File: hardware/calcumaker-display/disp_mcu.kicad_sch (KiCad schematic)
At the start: 8 parts, among them J3 SWD TC2030-NL, U4 STM32G031K8U6

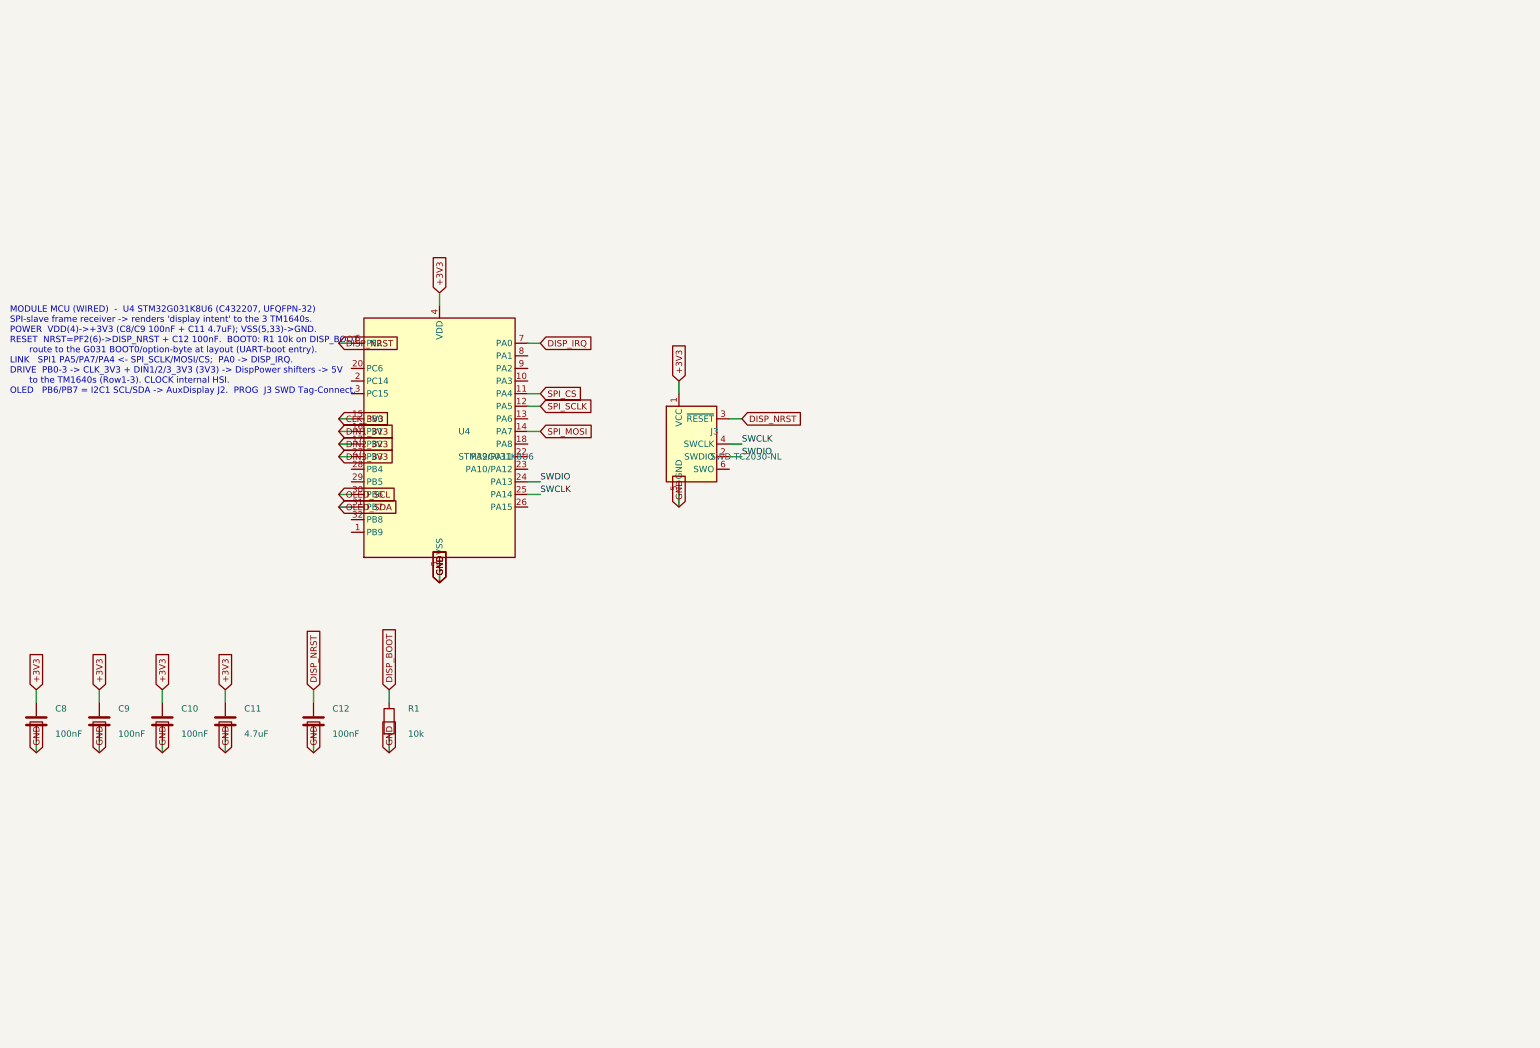
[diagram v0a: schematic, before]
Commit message: Floorplan both display PCBs and verify their schematic nets
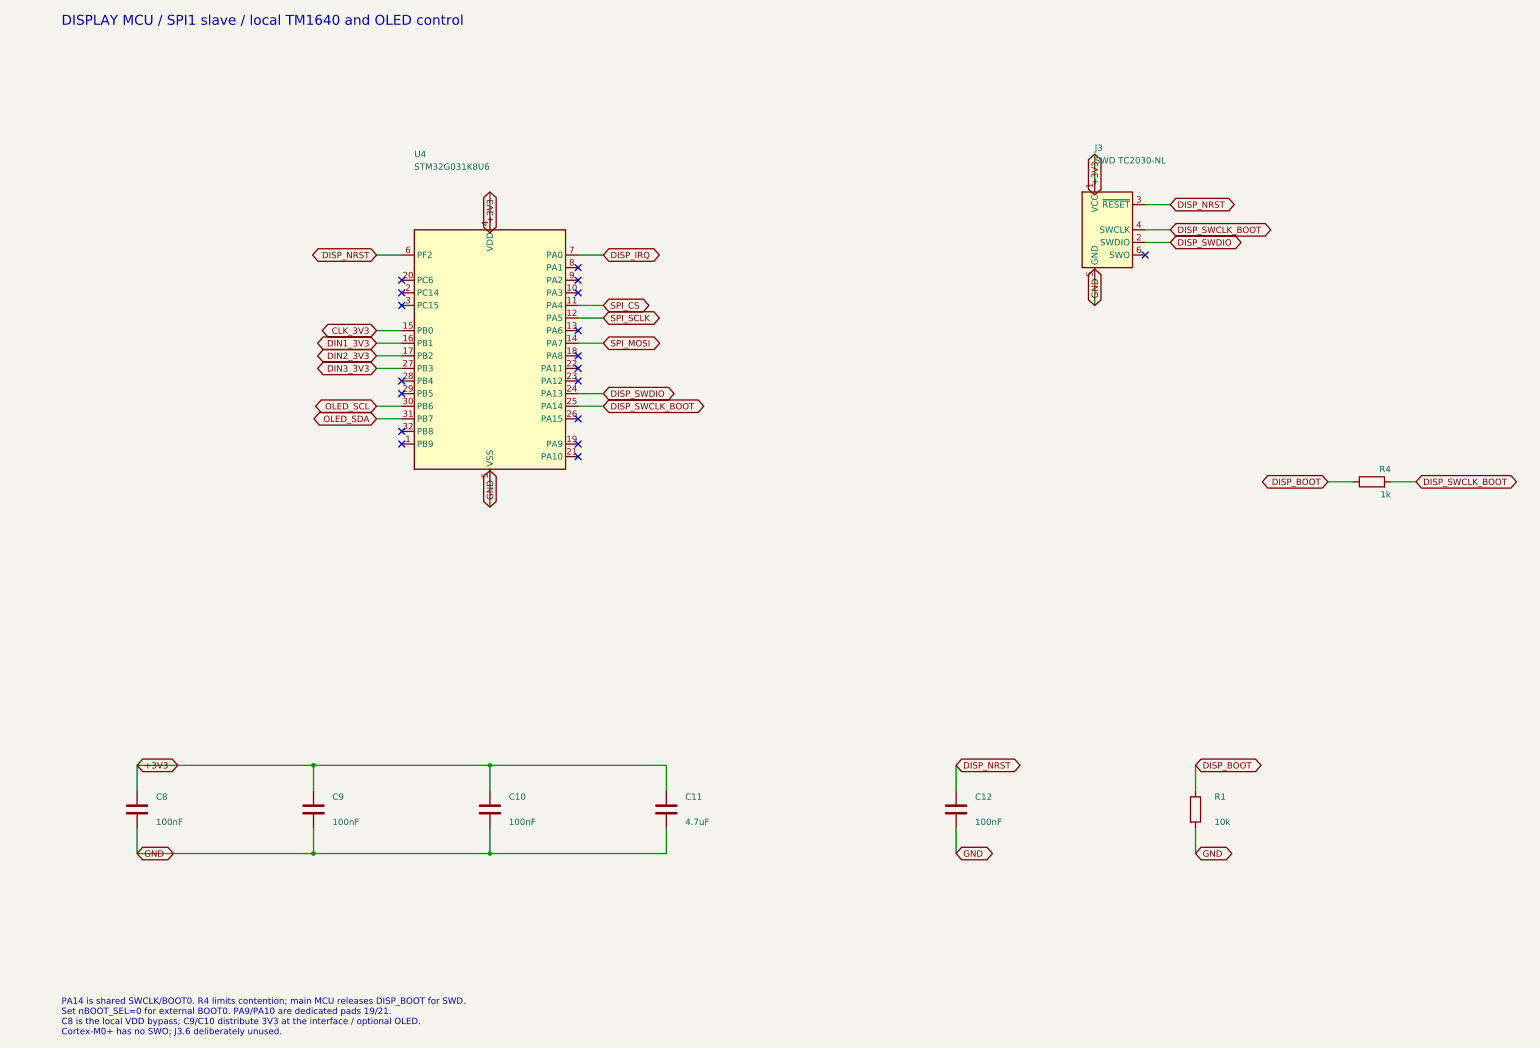
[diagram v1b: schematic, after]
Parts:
- added R4: 1k, Resistor_SMD:R_0402_1005Metric, symbol Device:R
- U4: symbol MCU_ST_STM32G0:STM32G031K8Ux -> calcumaker:STM32G031K8U6
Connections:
- net DISP_BOOT: now also R4.1
- net SWCLK renamed DISP_SWCLK_BOOT
- net DISP_SWCLK_BOOT: now also R4.2
- net SWDIO renamed DISP_SWDIO
- no-connect marks 0 -> 18
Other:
- note added: "DISPLAY MCU / SPI1 slave / local TM1640 and OLED control"
- note added: "PA14 is shared SWCLK/BOOT0. R4 limits contention; main MCU releases DISP_BOOT for SWD. Set nBOOT_SEL=0 for external BOOT0. PA9/PA10 are dedicated pads 19/21. C8 is the local VDD bypass; C9/C10 distribute 3V3 at the interface / optional OLED. Cortex-M0+ has no SWO; J3.6 deliberately unused."
- note removed: "MODULE MCU (WIRED) - U4 STM32G031K8U6 (C432207, UFQFPN-32) SPI-slave frame receiver -> renders 'display intent' to the 3 TM1640s. POWER VDD(4)->+3V3 (C8/C9 100nF + C11 4.7uF); VSS(5,33)->GND. RESET NRST=PF2(6)->DISP_NRST + C12 100nF. BOOT0: R1 10k on DISP_BOOT; route to the G031 BOOT0/option-byte at layout (UART-boot entry). LINK SPI1 PA5/PA7/PA4 <- SPI_SCLK/MOSI/CS; PA0 -> DISP_IRQ. DRIVE PB0-3 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"
- title: Calcumaker 16 — Display — Module MCU (STM32G031K8U6, SPI-slave) — wired -> Calcumaker 16 / display / disp mcu
- moved on the sheet: C10, C11, C12, C8, C9, J3, R1
